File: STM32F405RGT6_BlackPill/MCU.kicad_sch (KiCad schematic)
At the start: 31 parts, among them J1 Conn_01x04, U1 STM32F405RGTx, Y1 25Mhz, Y2 Crystal

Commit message: First version of the scheme
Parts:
- added D5: LED, symbol Device:LED
- added J3, J4: Conn_02x15_Odd_Even, Connector_PinHeader_2.54mm:PinHeader_2x15_P2.54mm_Vertical, symbol Connector_Generic:Conn_02x15_Odd_Even
- added R13: 5k1, symbol Device:R
- added R7: 10k, symbol Device:R
- added SW3: ~, symbol BlackPillLibrary:SW_PUSH_6mm_H5mm
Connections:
- net +3.3V: now also J3.25 (Pin_25), J3.27 (Pin_27), J3.29 (Pin_29), J4.27 (Pin_27), J4.29 (Pin_29), SW3.2
- net GND: now also D5.1 (K), J3.2 (Pin_2), J3.26 (Pin_26), J3.28 (Pin_28), J3.30 (Pin_30), J3.4 (Pin_4), J3.6 (Pin_6), J4.2 (Pin_2), J4.28 (Pin_28), J4.30 (Pin_30), R7.2
- net PB2: now also R13.1
- net PC2: now reaches U1.10 (PC2)
- net PC2: now also J3.9 (Pin_9)
- net PC3: now reaches U1.11 (PC3)
- net PC3: now also J3.10 (Pin_10)
- net PA0: now reaches U1.14 (PA0)
- net PA0: now also J3.11 (Pin_11)
- net PA1: now reaches U1.15 (PA1)
- net PA1: now also J3.12 (Pin_12)
- net PA2: now reaches U1.16 (PA2)
- net PA2: now also J3.13 (Pin_13)
- net PA3: now reaches U1.17 (PA3)
- net PA3: now also J3.14 (Pin_14)
- net PC13: now reaches U1.2 (PC13)
- net PC13: now also R7.1, SW3.1
- net PA4: now reaches U1.20 (PA4)
- net PA4: now also J3.15 (Pin_15)
- net PA5: now reaches U1.21 (PA5)
- net PA5: now also J3.16 (Pin_16)
- net PA6: now reaches U1.22 (PA6)
- net PA6: now also J3.17 (Pin_17)
- net PA7: now reaches U1.23 (PA7)
- net PA7: now also J3.18 (Pin_18)
- net PC4: now reaches U1.24 (PC4)
- net PC4: now also J3.19 (Pin_19)
- net PC5: now reaches U1.25 (PC5)
- net PC5: now also J3.20 (Pin_20)
- net PB0: now reaches U1.26 (PB0)
- net PB0: now also J3.21 (Pin_21)
- net PB1: now reaches U1.27 (PB1)
- net PB1: now also J3.22 (Pin_22)
- net PB10: now reaches U1.29 (PB10)
- net PB10: now also J3.23 (Pin_23)
- net PB11: now reaches U1.30 (PB11)
- net PB11: now also J3.24 (Pin_24)
- net PB12: now reaches U1.33 (PB12)
- net PB12: now also J4.26 (Pin_26)
- net PB13: now reaches U1.34 (PB13)
- net PB13: now also J4.25 (Pin_25)
- net PB14: now reaches U1.35 (PB14)
- net PB14: now also J4.24 (Pin_24)
- net PB15: now reaches U1.36 (PB15)
- net PB15: now also J4.23 (Pin_23)
- net PC6: now reaches U1.37 (PC6)
- net PC6: now also J4.22 (Pin_22)
- net PC7: now reaches U1.38 (PC7)
- net PC7: now also J4.21 (Pin_21)
- net PC8: now reaches U1.39 (PC8)
- net PC8: now also J4.20 (Pin_20)
- net PC9: now reaches U1.40 (PC9)
- net PC9: now also J4.19 (Pin_19)
- net PA8: now reaches U1.41 (PA8)
- net PA8: now also J4.18 (Pin_18)
- net PA9: now reaches U1.42 (PA9)
- net PA9: now also J4.15 (Pin_15)
- net PA10: now reaches U1.43 (PA10)
- net PA10: now also J4.16 (Pin_16)
- net PA15: now reaches U1.50 (PA15)
- net PA15: now also J4.13 (Pin_13)
- net PC10: now reaches U1.51 (PC10)
- net PC10: now also J4.14 (Pin_14)
- net PC11: now reaches U1.52 (PC11)
- net PC11: now also J4.11 (Pin_11)
- net PC12: now reaches U1.53 (PC12)
- net PC12: now also J4.12 (Pin_12)
- net PD2: now reaches U1.54 (PD2)
- net PD2: now also J4.10 (Pin_10)
- net PB3: now reaches U1.55 (PB3)
- net PB3: now also J4.9 (Pin_9)
- net PB4: now reaches U1.56 (PB4)
- net PB4: now also J4.8 (Pin_8)
- net PB5: now reaches U1.57 (PB5)
- net PB5: now also J4.7 (Pin_7)
- net PB6: now reaches U1.58 (PB6)
- net PB6: now also J4.6 (Pin_6)
- net PB7: now reaches U1.59 (PB7)
- net PB7: now also J4.5 (Pin_5)
- net PB8: now reaches U1.61 (PB8)
- net PB8: now also J4.4 (Pin_4)
- net PB9: now reaches U1.62 (PB9)
- net PB9: now also J4.3 (Pin_3)
- net PC0: now reaches U1.8 (PC0)
- net PC0: now also J3.7 (Pin_7)
- net PC1: now reaches U1.9 (PC1)
- net PC1: now also J3.8 (Pin_8)
- new net: D5.2 (A), R13.2
- new net +5V: J3.1 (Pin_1), J3.3 (Pin_3), J3.5 (Pin_5), J4.1 (Pin_1)
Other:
- note added: "User Key"
- note added: "User LED"
- moved on the sheet: C4, C6, U1

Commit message: Essential part of the BOM fill
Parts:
- removed C10: 1u, symbol Device:C
- removed C11: 10n, symbol Device:C
- removed L1: 39n, symbol Device:L
- removed Y2: Crystal, symbol Device:Crystal
- added C107: 10n, Capacitor_SMD:C_0402_1005Metric, symbol Device:C
- added C108, C109: 1u, Capacitor_SMD:C_0603_1608Metric, symbol Device:C
- added L100: 10n, Inductor_SMD:L_0402_1005Metric, symbol Device:L
- added R104: 47R, Resistor_SMD:R_0402_1005Metric, symbol Device:R
- added Y1: 32768Hz, Crystal:Crystal_SMD_3225-4Pin_3.2x2.5mm, symbol Device:Crystal_GND24
- C100: renamed from C1; footprint (none) -> Capacitor_SMD:C_0402_1005Metric
- C101: renamed from C2; footprint (none) -> Capacitor_SMD:C_0603_1608Metric
- C102: renamed from C3; footprint (none) -> Capacitor_SMD:C_0402_1005Metric
- C103: renamed from C5; footprint (none) -> Capacitor_SMD:C_0402_1005Metric
- C104: renamed from C7; footprint (none) -> Capacitor_SMD:C_0402_1005Metric
- C105: renamed from C8; footprint (none) -> Capacitor_SMD:C_0402_1005Metric
- C106: renamed from C9; footprint (none) -> Capacitor_SMD:C_0402_1005Metric
- C110: renamed from C12; value 12p -> 15p; footprint (none) -> Capacitor_SMD:C_0402_1005Metric
- C111: renamed from C13; value 12p -> 15p; footprint (none) -> Capacitor_SMD:C_0402_1005Metric
- C112: renamed from C14; value 1p5 -> 15p; footprint (none) -> Capacitor_SMD:C_0402_1005Metric
- C113: renamed from C15; value 1p5 -> 15p; footprint (none) -> Capacitor_SMD:C_0402_1005Metric
- C114: renamed from C4; footprint (none) -> Capacitor_SMD:C_0805_2012Metric
- C115: renamed from C6; footprint (none) -> Capacitor_SMD:C_0805_2012Metric
- D103: renamed from D5; footprint (none) -> LED_SMD:LED_0603_1608Metric
- R100: renamed from R1; footprint (none) -> Resistor_SMD:R_0402_1005Metric
- R101: renamed from R2; footprint (none) -> Resistor_SMD:R_0402_1005Metric
- R102: renamed from R5; footprint (none) -> Resistor_SMD:R_0402_1005Metric
- R103: renamed from R6; value 47 -> 47R; footprint (none) -> Resistor_SMD:R_0402_1005Metric
- R105: renamed from R3; value 49R9 -> 47R
- R106: renamed from R4; value 49R9 -> 47R
- R107: renamed from R7; footprint (none) -> Resistor_SMD:R_0402_1005Metric
- R108: renamed from R13; footprint (none) -> Resistor_SMD:R_0402_1005Metric
- SW100: renamed from SW1; footprint (none) -> Button_Switch_THT:SW_PUSH_6mm
- SW101: renamed from SW2; footprint (none) -> Button_Switch_THT:SW_PUSH_6mm
- SW102: renamed from SW3; footprint (none) -> Button_Switch_THT:SW_PUSH_6mm
- U100: renamed from U1; footprint Package_CSP:ST_WLCSP-90_Die413 -> Package_QFP:LQFP-64_10x10mm_P0.5mm; DigiKey Part Number (none) -> 497-11767-ND; Manufacturer (none) -> STMicroelectronics; Manufacturer Product Number (none) -> STM32F405RGT6
- Y100: renamed from Y1; footprint (none) -> Crystal:Crystal_SMD_3225-4Pin_3.2x2.5mm; DigiKey Part Number (none) -> 535-ASE-25.000MHZ-L-C-TDKR-ND; Manufacturer (none) -> Abracon LLC; Manufacturer Product Number (none) -> ASE-25.000MHZ-L-C-T
- renumbered D1 to D100, D2 to D101, D3 to D102, J1 to J100, J3 to J101, J4 to J102
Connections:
- net +3.3VA: now also C107.1, C108.1, L100.1
- net +3V3: now also C109.1, L100.2
- net GND: now also J102.17 (Pin_17), C107.2, C108.2, C109.2, Y1.2, Y1.4
- net OSC32_IN: now also R104.1; no longer C113.1
- net OSC32_OUT: now also Y1.1
- new net: C113.1, R104.2, Y1.3
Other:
- note added: "Cload=2*(CL-Cstray)=2*(15-[2:7])=15"
- note removed: "Cload=2*(CL-Cstray)"
- moved on the sheet: C113

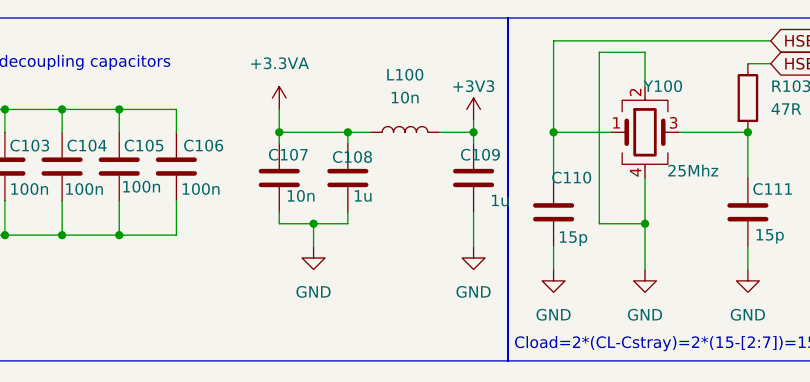
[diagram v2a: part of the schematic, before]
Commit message: BOM table fill
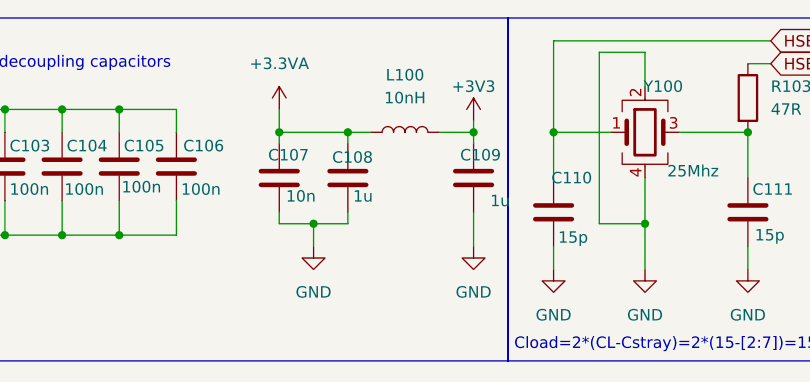
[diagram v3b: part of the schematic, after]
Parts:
- C100, C102, C103, C104, C105, C106: DigiKey Part Number (none) -> 1276-1002-6-ND; Manufacturer (none) -> Samsung Electro-Mechanics; Manufacturer Product Number (none) -> CL05B104KP5NNNC
- C101: DigiKey Part Number (none) -> 1276-1044-6-ND; Manufacturer (none) -> Samsung Electro-Mechanics; Manufacturer Product Number (none) -> CL10A475KP8NNNC
- C107: DigiKey Part Number (none) -> 1276-1028-6-ND; Manufacturer (none) -> Samsung Electro-Mechanics; Manufacturer Product Number (none) -> CL05B103KB5NNNC
- C108, C109: DigiKey Part Number (none) -> 1276-1946-6-ND; Manufacturer (none) -> Samsung Electro-Mechanics; Manufacturer Product Number (none) -> CL10B105KP8NNNC
- C110, C111, C112, C113: DigiKey Part Number (none) -> 490-11191-6-ND; Manufacturer (none) -> Murata Electronics; Manufacturer Product Number (none) -> GJM1555C1H150FB01D
- C114, C115: DigiKey Part Number (none) -> 445-1420-6-ND; Manufacturer (none) -> TDK Corporation; Manufacturer Product Number (none) -> C2012X7R1C225K125AB
- D100, D101, D102: DigiKey Part Number (none) -> 1727-3825-6-ND; Manufacturer (none) -> Nexperia USA Inc.; Manufacturer Product Number (none) -> PESD3V3L1BA,115
- D103: DigiKey Part Number (none) -> 732-4971-6-ND; Manufacturer (none) -> Würth Elektronik; Manufacturer Product Number (none) -> 150060GS75000
- L100: value 10n -> 10nH; DigiKey Part Number (none) -> 712-LRC0402CJ10NGV001TDKR-ND; Manufacturer (none) -> Johanson Technology Inc.; Manufacturer Product Number (none) -> LRC0402CJ10NGV001T
- R100, R101, R102, R107: DigiKey Part Number (none) -> 1276-3431-6-ND; Manufacturer (none) -> Samsung Electro-Mechanics; Manufacturer Product Number (none) -> RC1005F103CS
- R103, R104, R105, R106: DigiKey Part Number (none) -> P47JDKR-ND; Manufacturer (none) -> Panasonic Electronic Components; Manufacturer Product Number (none) -> ERJ-2GEJ470X
- R108: DigiKey Part Number (none) -> P5.1KDCDKR-ND; Manufacturer (none) -> Panasonic Electronic Components; Manufacturer Product Number (none) -> ERA-2AEB512X

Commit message: Initial components placement
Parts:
- J100: footprint Connector_PinHeader_2.54mm:PinHeader_1x04_P2.54mm_Horizontal -> Connector_PinHeader_2.54mm:PinHeader_1x04_P2.54mm_Vertical
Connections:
- net HSE_IN: now also C110.1, Y100.1; no longer R103.1
- net HSE_OUT: now also R103.1; no longer C110.1, Y100.1
- net OSC32_IN: now also C112.1, Y1.1; no longer R104.1
- net OSC32_OUT: now also R104.1; no longer C112.1, Y1.1
- net VCAP_1: now reaches C114.1, U100.31 (VCAP_1)
- net XTAL32_IN: now reaches C113.1, R104.2, Y1.3
- net VCAP_2: now reaches C115.1, U100.47 (VCAP_2)
- net XTAL_IN: now reaches C111.1, R103.2, Y100.3
- net SWDIO_CONN: now reaches D101.1 (A1), J100.3 (Pin_3), R105.1
- net SWCLK_CONN: now reaches D102.1 (A1), J100.2 (Pin_2), R106.1
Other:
- moved on the sheet: C115, Y100

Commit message: Signal routing (bottom part)
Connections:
- net +3V3 is gone; now on net +3.3V: C109.1, D100.1 (A1), J100.4 (Pin_4), L100.2
- net +3.3V: now also J101.2 (Pin_2); no longer J101.25 (Pin_25), J101.27 (Pin_27), J101.29 (Pin_29)
- net +5V: now also J101.30 (Pin_30); no longer J101.1 (Pin_1), J101.3 (Pin_3), J101.5 (Pin_5)
- net GND: now also J101.1 (Pin_1), J101.29 (Pin_29); no longer J101.2 (Pin_2), J101.26 (Pin_26), J101.28 (Pin_28), J101.30 (Pin_30), J101.4 (Pin_4), J101.6 (Pin_6)
- net PA0: now also J101.8 (Pin_8); no longer J101.11 (Pin_11)
- net PA1: now also J101.7 (Pin_7); no longer J101.12 (Pin_12)
- net PA2: now also J101.10 (Pin_10); no longer J101.13 (Pin_13)
- net PA3: now also J101.9 (Pin_9); no longer J101.14 (Pin_14)
- net PA4: now also J101.12 (Pin_12); no longer J101.15 (Pin_15)
- net PA5: now also J101.11 (Pin_11); no longer J101.16 (Pin_16)
- net PA6: now also J101.14 (Pin_14); no longer J101.17 (Pin_17)
- net PA7: now also J101.13 (Pin_13); no longer J101.18 (Pin_18)
- net PB0: now also J101.18 (Pin_18); no longer J101.21 (Pin_21)
- net PB1: now also J101.17 (Pin_17); no longer J101.22 (Pin_22)
- net PB10: now also J101.20 (Pin_20); no longer J101.23 (Pin_23)
- net PB11: now also J101.19 (Pin_19); no longer J101.24 (Pin_24)
- net PB12: now also J101.22 (Pin_22); no longer J102.26 (Pin_26)
- net PB13: now also J101.21 (Pin_21); no longer J102.25 (Pin_25)
- net PB14: now also J101.24 (Pin_24); no longer J102.24 (Pin_24)
- net PB15: now also J101.23 (Pin_23); no longer J102.23 (Pin_23)
- net PC0: now also J101.4 (Pin_4); no longer J101.7 (Pin_7)
- net PC1: now also J101.3 (Pin_3); no longer J101.8 (Pin_8)
- net PC2: now also J101.6 (Pin_6); no longer J101.9 (Pin_9)
- net PC3: now also J101.5 (Pin_5); no longer J101.10 (Pin_10)
- net PC4: now also J101.16 (Pin_16); no longer J101.19 (Pin_19)
- net PC5: now also J101.15 (Pin_15); no longer J101.20 (Pin_20)
- net PC6: now also J101.26 (Pin_26); no longer J102.22 (Pin_22)
- net PC7: now also J101.25 (Pin_25); no longer J102.21 (Pin_21)
- net PC8: now also J101.28 (Pin_28); no longer J102.20 (Pin_20)
- net PC9: now also J101.27 (Pin_27); no longer J102.19 (Pin_19)
- no-connect marks 0 -> 7

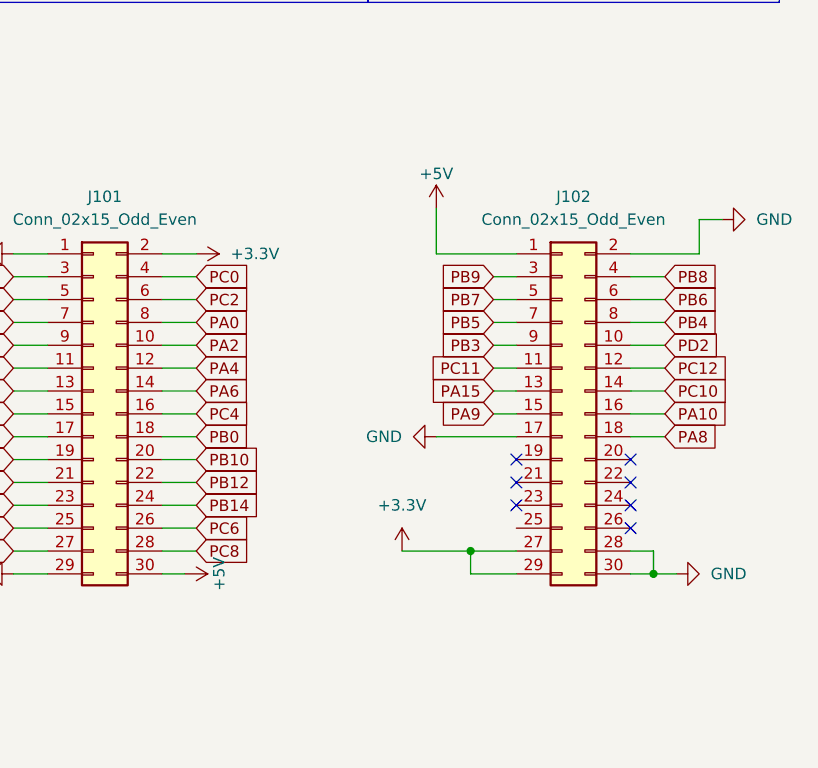
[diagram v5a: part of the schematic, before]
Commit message: Signal routing (upper part)
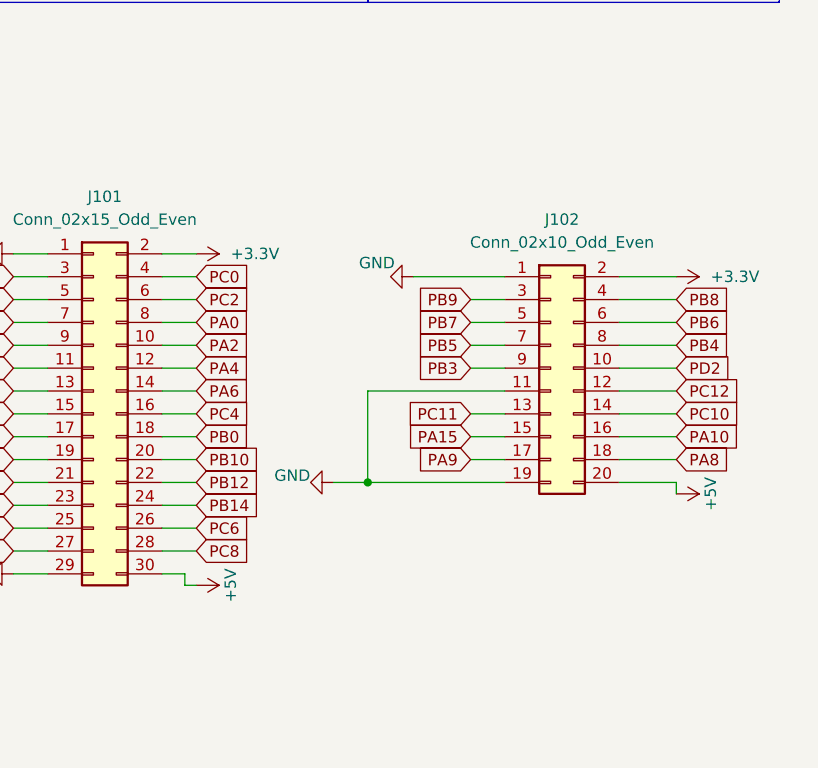
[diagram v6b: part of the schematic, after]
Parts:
- removed J102: Conn_02x15_Odd_Even, Connector_PinHeader_2.54mm:PinHeader_2x15_P2.54mm_Vertical, symbol Connector_Generic:Conn_02x15_Odd_Even
- added J102: Conn_02x10_Odd_Even, Connector_PinHeader_2.54mm:PinHeader_2x10_P2.54mm_Vertical, symbol Connector_Generic:Conn_02x10_Odd_Even
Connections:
- net +3.3V: now also J102.2 (Pin_2)
- net +5V: now also J102.20 (Pin_20)
- net GND: now also J102.1 (Pin_1), J102.11 (Pin_11), J102.19 (Pin_19)
- net PA10: now also J102.16 (Pin_16)
- net PA15: now also J102.15 (Pin_15)
- net PA8: now also J102.18 (Pin_18)
- net PA9: now also J102.17 (Pin_17)
- net PB3: now also J102.9 (Pin_9)
- net PB4: now also J102.8 (Pin_8)
- net PB5: now also J102.7 (Pin_7)
- net PB6: now also J102.6 (Pin_6)
- net PB7: now also J102.5 (Pin_5)
- net PB8: now also J102.4 (Pin_4)
- net PB9: now also J102.3 (Pin_3)
- net PC10: now also J102.14 (Pin_14)
- net PC11: now also J102.13 (Pin_13)
- net PC12: now also J102.12 (Pin_12)
- net PD2: now also J102.10 (Pin_10)
- no-connect marks 7 -> 0
